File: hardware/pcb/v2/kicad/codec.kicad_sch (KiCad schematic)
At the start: 22 parts, among them U1 TLV320AIC3104IRHBR, U2 XC6206P182MR

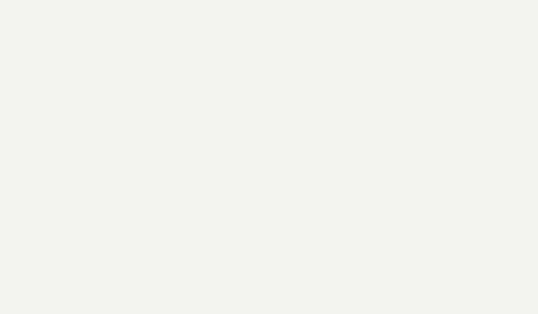
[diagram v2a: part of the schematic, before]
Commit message: feat(hardware): verify LCSC parts, unify 100nF to 50V, move J1 to top
BOM verification pass on PCB v2:
- Fixed 3 wrong LCSC numbers (C5/C6 15pF, C10/C31 1uF, C12-C35/C56 100nF size)
- Filled 16 missing LCSC numbers across codec and ringer sub-sheets
- Unified all 100nF 0402 caps to C307331 (50V) since C54 is on +12V
- C55 updated to C336270 (47uF 25V Panasonic, D5xL5.8 — 2x derating for 12V rail)
- R5/R11 updated to in-stock C60490 (Yageo 10k 0402)
- COMPONENTS.md aligned with schematic

J1 body moved from B.Cu to F.Cu for Pi face-down mounting:
- Direct layer-string swap (B.Cu/SilkS/Fab/CrtYd -> F.*) without any
  coordinate mirror, so all 40 pin positions and routed traces stay
  intact. Removed stale (justify mirror) attributes from text fields.

DRC: 0 unconnected, 0 dangling, 0 clearance. Remaining 48 violations
are all cosmetic (silk + library drift).
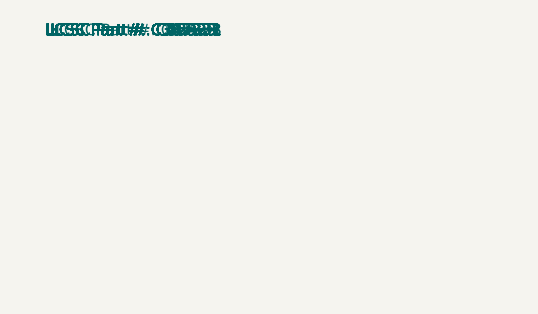
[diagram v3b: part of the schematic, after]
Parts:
- C1, C13, C14, C15, C16, C17, C3, C5, C6, C7, C8: LCSC Part # (none) -> C307331
- C10, C2: LCSC Part # (none) -> C15525
- C11, C12: LCSC Part # (none) -> C47339
- C18: LCSC Part # (none) -> C1523
- C4, C9: LCSC Part # (none) -> C52923
- R1: LCSC Part # (none) -> C25879
- R2: LCSC Part # (none) -> C60490
- U1: LCSC Part # (none) -> C181753
- U2: LCSC Part # (none) -> C347373
